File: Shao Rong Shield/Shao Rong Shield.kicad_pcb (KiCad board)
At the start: 2 copper layers, 68.6 x 53.3 mm, 16 parts, among them J1 Power, J10 VIBRATION MOTOR, J11 SPARE1, J12 SPARE2, J2 Digital/PWM, J3 Analog, J4 Digital/PWM, J5 POWER SUPPLY, J6 STEPPER MOTOR, J7 KEYBOARD, J8 LCD, J9 RS232

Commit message: organised pcb
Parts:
- moved J8 18.2 mm to (136.2, 60.8)
- moved J7 18.1 mm to (147.1, 60.8)
- moved J10 14.2 mm to (125.4, 60.8)
- moved J11 6.02 mm to (148.0, 80.0)
- moved J12 3.61 mm to (158.5, 80.0)
- moved J9 1.52 mm to (158.0, 63.2)
- moved J6 1.03 mm to (115.0, 60.8)
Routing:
- net +5V: track 0.11 -> 43.7 mm
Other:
- board text added: "5V"
- board text added: "Gnd"
- board text removed: "ICSP"
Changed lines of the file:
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@@
 		(tags "connector JST XH horizontal")
 		(property "Reference" "J5"
-			(at 1.25 -3.5 90)
-			(layer "F.SilkS")
+			(at 1.25 3.45 90)
+			(layer "F.Fab")
 			(effects
 				(font
@@
 		)
 		(property "Value" "POWER SUPPLY"
-			(at 1.25 10.4 90)
-			(layer "F.Fab")
+			(at 1.75 -5.05 90)
+			(layer "F.SilkS")
+			(hide yes)
 			(effects
 				(font
@@
 	(footprint "Connector_JST:JST_XH_B3B-XH-A_1x03_P2.50mm_Vertical"
 		(layer "F.Cu")
-		(at 147.5 74 -90)
+		(at 148 80 -90)
 		(descr "JST XH series connector, B3B-XH-A (http://www.jst-mfg.com/product/pdf/eng/eXH.pdf), generated with kicad-footprint-generator")
 		(tags "connector JST XH vertical")
 		(property "Reference" "J11"
 			(at 2.5 -3.55 90)
-			(layer "F.SilkS")
+			(layer "Edge.Cuts")
 			(effects
 				(font
@@
 		(property "Value" "SPARE1"
 			(at 2.5 4.6 90)
-			(layer "F.Fab")
+			(layer "F.SilkS")
 			(effects
 				(font
@@
 	(footprint "Connector_JST:JST_XH_B6B-XH-A_1x06_P2.50mm_Vertical"
 		(layer "F.Cu")
-		(at 114 60.5 -90)
+		(at 115 60.75 -90)
 		(descr "JST XH series connector, B6B-XH-A (http://www.jst-mfg.com/product/pdf/eng/eXH.pdf), generated with kicad-footprint-generator")
 		(tags "connector JST XH vertical")
 		(property "Reference" "J6"
 			(at 6.25 -3.55 90)
-			(layer "F.SilkS")
+			(layer "F.Fab")
 			(effects
 				(font
@@
 		)
 		(property "Value" "STEPPER MOTOR"
-			(at 6.25 4.6 90)
-			(layer "F.Fab")
+			(at 2.130953 4.6 90)
+			(layer "F.SilkS")
 			(effects
 				(font
@@
 	(footprint "Connector_JST:JST_XH_B3B-XH-A_1x03_P2.50mm_Vertical"
 		(layer "F.Cu")
-		(at 156.5 83 -90)
+		(at 158.5 80 -90)
 		(descr "JST XH series connector, B3B-XH-A (http://www.jst-mfg.com/product/pdf/eng/eXH.pdf), generated with kicad-footprint-generator")
 		(tags "connector JST XH vertical")
 		(property "Reference" "J12"
 			(at 2.5 -3.55 90)
-			(layer "F.SilkS")
+			(layer "F.Fab")
 			(effects
 				(font
@@
 		(property "Value" "SPARE2"
 			(at 2.5 4.6 90)
-			(layer "F.Fab")
+			(layer "F.SilkS")
 			(effects
 				(font
@@
 	(footprint "Connector_JST:JST_XH_B3B-XH-A_1x03_P2.50mm_Vertical"
 		(layer "F.Cu")
-		(at 129.025 60.5 -90)
+		(at 147.121875 60.75 -90)
 		(descr "JST XH series connector, B3B-XH-A (http://www.jst-mfg.com/product/pdf/eng/eXH.pdf), generated with kicad-footprint-generator")
 		(tags "connector JST XH vertical")
 		(property "Reference" "J7"
 			(at 2.5 -3.55 90)
-			(layer "F.SilkS")
+			(layer "F.Fab")
 			(effects
 				(font
@@
 		)
 		(property "Value" "KEYBOARD"
-			(at 2.5 4.6 90)
-			(layer "F.Fab")
+			(at -0.178571 4.6 90)
+			(layer "F.SilkS")
 			(effects
 				(font
@@
 	(footprint "Connector_JST:JST_XH_B4B-XH-A_1x04_P2.50mm_Vertical"
 		(layer "F.Cu")
-		(at 129 77.5 -90)
+		(at 136.24375 60.75 -90)
 		(descr "JST XH series connector, B4B-XH-A (http://www.jst-mfg.com/product/pdf/eng/eXH.pdf), generated with kicad-footprint-generator")
 		(tags "connector JST XH vertical")
 		(property "Reference" "J8"
 			(at 3.75 -3.55 90)
-			(layer "F.SilkS")
+			(layer "F.Fab")
 			(effects
 				(font
@@
 		)
 		(property "Value" "LCD"
-			(at 3.75 4.6 90)
-			(layer "F.Fab")
+			(at -2.607143 4.6 90)
+			(layer "F.SilkS")
 			(effects
 				(font
@@
 	(footprint "Connector_JST:JST_XH_B3B-XH-A_1x03_P2.50mm_Vertical"
 		(layer "F.Cu")
-		(at 139.525 60.5 -90)
+		(at 125.365625 60.75 -90)
 		(descr "JST XH series connector, B3B-XH-A (http://www.jst-mfg.com/product/pdf/eng/eXH.pdf), generated with kicad-footprint-generator")
 		(tags "connector JST XH vertical")
 		(property "Reference" "J10"
 			(at 2.5 -3.55 90)
-			(layer "F.SilkS")
+			(layer "F.Fab")
 			(effects
 				(font
@@
 		)
 		(property "Value" "VIBRATION MOTOR"
-			(at 2.5 4.6 90)
-			(layer "F.Fab")
+			(at 2.630952 4.6 90)
+			(layer "F.SilkS")
 			(effects
 				(font
@@
 	(footprint "Connector_JST:JST_XH_B3B-XH-A_1x03_P2.50mm_Vertical"
 		(layer "F.Cu")
-		(at 159.5 63 -90)
+		(at 158 63.25 -90)
 		(descr "JST XH series connector, B3B-XH-A (http://www.jst-mfg.com/product/pdf/eng/eXH.pdf), generated with kicad-footprint-generator")
 		(tags "connector JST XH vertical")
 		(property "Reference" "J9"
 			(at 2.5 -3.55 90)
-			(layer "F.SilkS")
+			(layer "F.Fab")
 			(effects
 				(font
@@
 		)
 		(property "Value" "RS232"
-			(at 2.5 4.6 90)
-			(layer "F.Fab")
+			(at -1.607143 4.6 90)
+			(layer "F.SilkS")
 			(effects
 				(font
@@
 	)
 	(gr_line
-		(start 98.095 96.825)
-		(end 98.095 87.935)
-		(stroke
-			(width 0.15)
-			(type solid)
-		)
-		(layer "Dwgs.User")
-	)
-	(gr_line
-		(start 111.43 96.825)
-		(end 98.095 96.825)
-		(stroke
-			(width 0.15)
-			(type solid)
-		)
-		(layer "Dwgs.User")
-	)
-	(gr_rect
-		(start 162.357 68.25)
-		(end 167.437 75.87)
-		(stroke
-			(width 0.15)
-			(type solid)
-		)
-		(fill none)
-		(layer "Dwgs.User")
-	)
-	(gr_line
-		(start 98.095 87.935)
-		(end 111.43 87.935)
-		(stroke
-			(width 0.15)
-			(type solid)
-		)
-		(layer "Dwgs.User")
-	)
-	(gr_line
-		(start 93.65 67.615)
-		(end 93.65 56.185)
-		(stroke
-			(width 0.15)
-			(type solid)
-		)
-		(layer "Dwgs.User")
-	)
-	(gr_line
-		(start 111.43 87.935)
-		(end 111.43 96.825)
-		(stroke
-			(width 0.15)
-			(type solid)
-		)
-		(layer "Dwgs.User")
-	)
-	(gr_line
-		(start 109.525 56.185)
-		(end 109.525 67.615)
-		(stroke
-			(width 0.15)
-			(type solid)
-		)
-		(layer "Dwgs.User")
-	)
-	(gr_line
-		(start 93.65 56.185)
-		(end 109.525 56.185)
-		(stroke
-			(width 0.15)
-			(type solid)
-		)
-		(layer "Dwgs.User")
-	)
-	(gr_line
-		(start 109.525 67.615)
-		(end 93.65 67.615)
-		(stroke
-			(width 0.15)
-			(type solid)
-		)
-		(layer "Dwgs.User")
-	)
-	(gr_line
 		(start 166.04 59.36)
 		(end 168.58 61.9)
@@
 		(layer "Edge.Cuts")
 	)
-	(gr_text "ICSP"
-		(at 164.897 72.06 90)
-		(layer "Dwgs.User")
+	(gr_text "Gnd"
+		(at 107 64.5 90)
+		(layer "F.SilkS")
+		(effects
+			(font
+				(size 1 1)
+				(thickness 0.15)
+			)
+			(justify left bottom)
+		)
+	)
+	(gr_text "5V"
+		(at 107 61.5 90)
+		(layer "F.SilkS")
 		(effects
 			(font
@@
 				(thickness 0.15)
 			)
+			(justify left bottom)
 		)
 	)
 	(segment
-		(start 118.96 67.54)
-		(end 119 67.5)
-		(width 0.25)
+		(start 125.365625 60.75)
+		(end 136.24375 60.75)
+		(width 0.2)
 		(layer "F.Cu")
 		(net 3)
 	)
 	(segment
-		(start 118.96 67.54)
-		(end 119 67.5)
-		(width 0.25)
-		(layer "B.Cu")
+		(start 103.45 60.75)
+		(end 115 60.75)
+		(width 0.2)
+		(layer "F.Cu")
+		(net 3)
+	)
+	(segment
+		(start 115 60.75)
+		(end 125.365625 60.75)
+		(width 0.2)
+		(layer "F.Cu")
+		(net 3)
+	)
+	(segment
+		(start 136.24375 60.75)
+		(end 147.121875 60.75)
+		(width 0.2)
+		(layer "F.Cu")
 		(net 3)
 	)

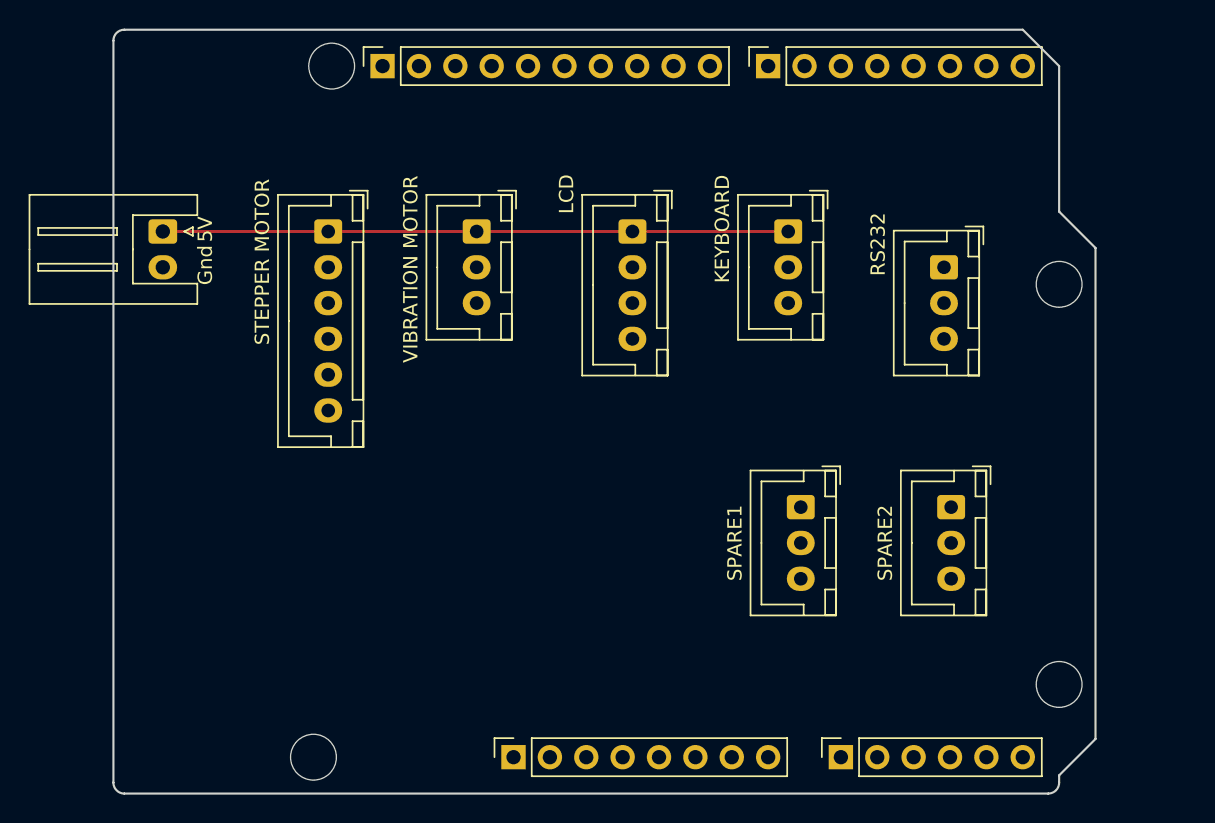
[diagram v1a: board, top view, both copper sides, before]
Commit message: Completed Shaorong and A4988 Shield
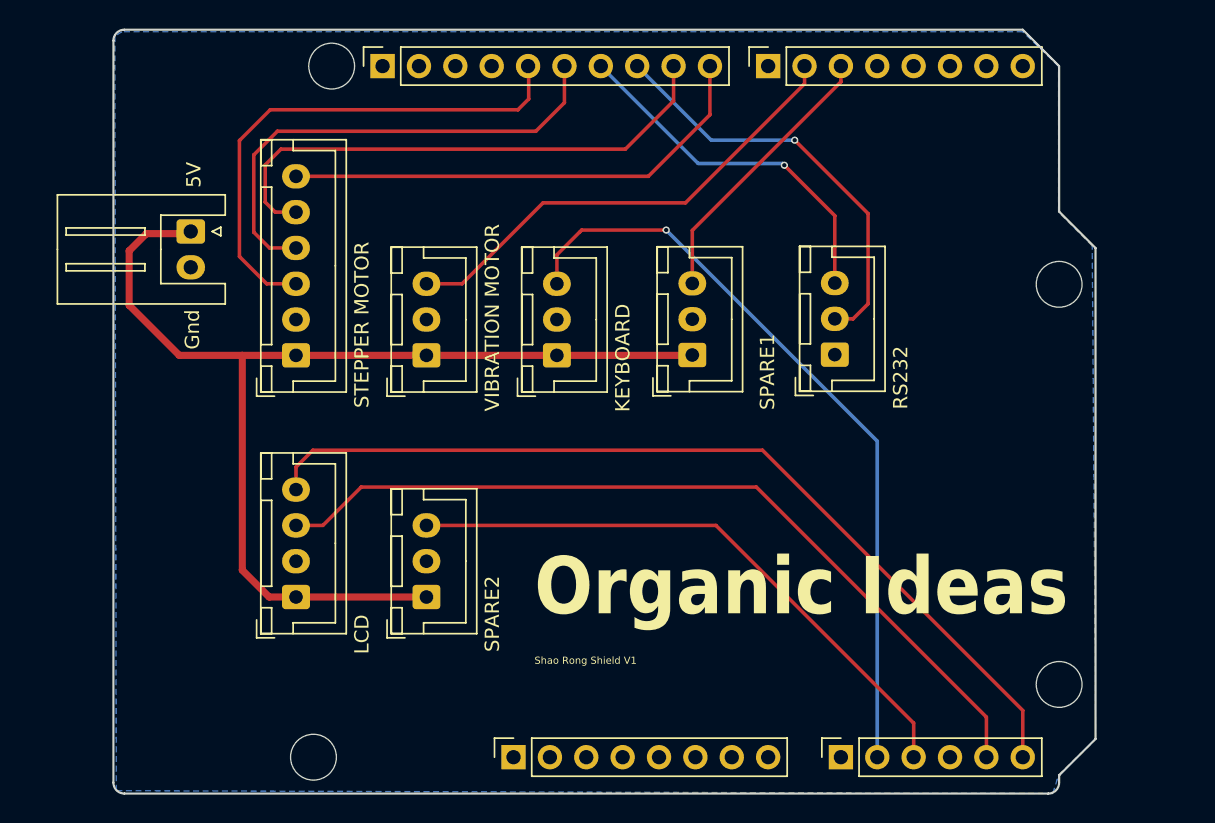
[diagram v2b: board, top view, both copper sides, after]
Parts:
- moved J12 37.2 mm to (121.9, 86.3), turned to 90 degrees
- moved J8 34.7 mm to (112.8, 86.3), turned to 90 degrees
- moved J7 18.3 mm to (131.0, 69.4), turned to 90 degrees
- moved J11 13.0 mm to (140.4, 69.4), turned to 90 degrees
- moved J9 9.76 mm to (150.4, 69.3), turned to 90 degrees
- moved J10 9.33 mm to (121.9, 69.4), turned to 90 degrees
- moved J6 8.94 mm to (112.8, 69.4), turned to 90 degrees
- moved J5 1.95 mm to (105.4, 60.8)
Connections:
- J2 pad 1: /SCL/A5 -> unconnected-(J2-Pin_1-Pad1)
- J2 pad 2: /SDA -> unconnected-(J2-Pin_2-Pad2)
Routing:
- net /SCL/A5: track 0.29 -> 64.3 mm
- net /SDA: track 0.00 -> 58.8 mm
- net /A1: track 0.00 -> 53.3 mm, vias 0 -> 1
- net /A2: track 0.00 -> 42.1 mm
- net /*9: track 0.00 -> 37.8 mm
- net /13: track 0.00 -> 36.6 mm
- net /12: track 0.00 -> 34.6 mm
- net +5V: track 43.7 -> 78.1 mm
- net /8: track 0.00 -> 34.3 mm
- net /*6: track 0.00 -> 33.4 mm
- net /*10: track 0.00 -> 29.5 mm, vias 0 -> 1
- net /*11: track 0.00 -> 25.4 mm, vias 0 -> 1
- net /*5: track 0.00 -> 19.5 mm
- added copper zone on B.Cu, net GND
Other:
- board text added: "Designed by Jeremy"
- board text added: "Organic Ideas"
- board text added: "Shao Rong Shield V1"
